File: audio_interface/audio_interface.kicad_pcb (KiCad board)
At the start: 2 copper layers, 139.7 x 81.3 mm, 152 parts, among them J1 XLR3, J10 MIC_EXT, J11 INST_EXT, J13 Test Headers, J14 SWD, J15 PCM_Jumper, J16 USB_B, J2 AudioJack2, J3 EXT_9V, J4 PROBE_GND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

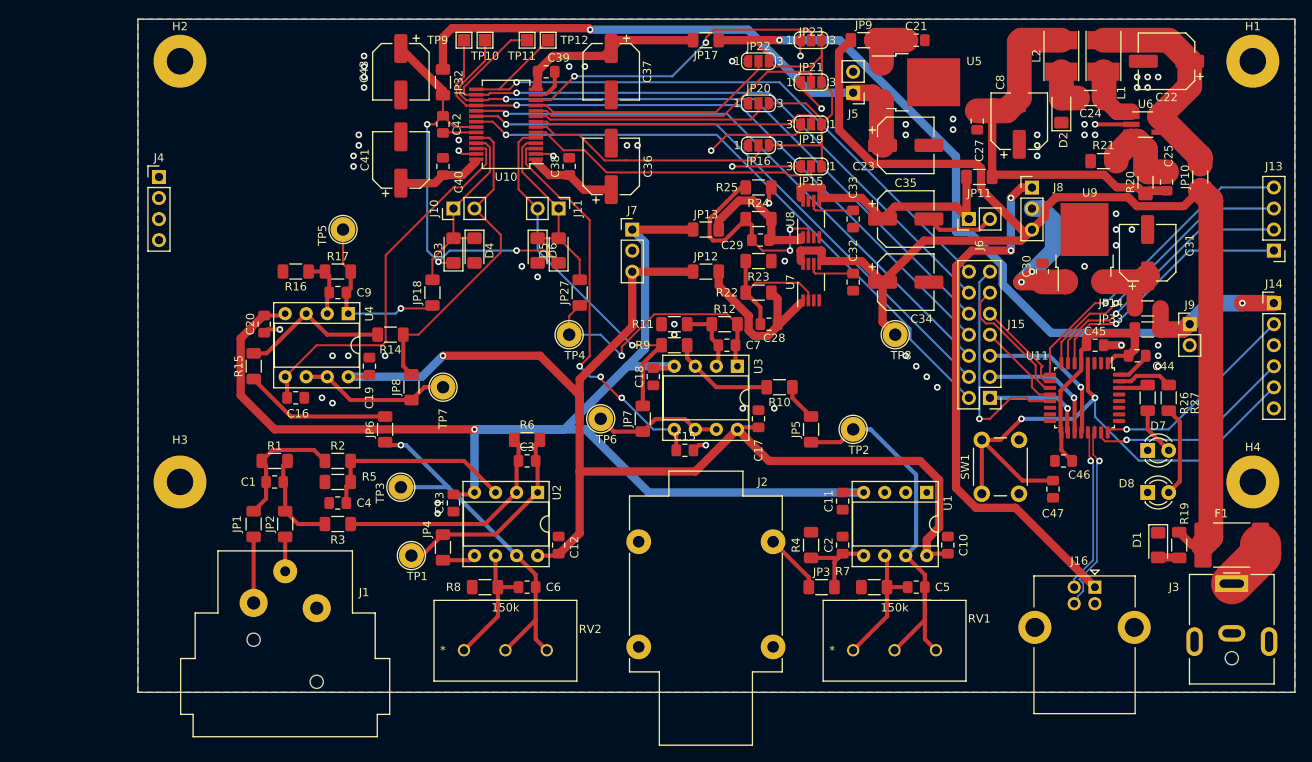
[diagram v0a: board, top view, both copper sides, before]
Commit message: Changed some footprints and grounding.
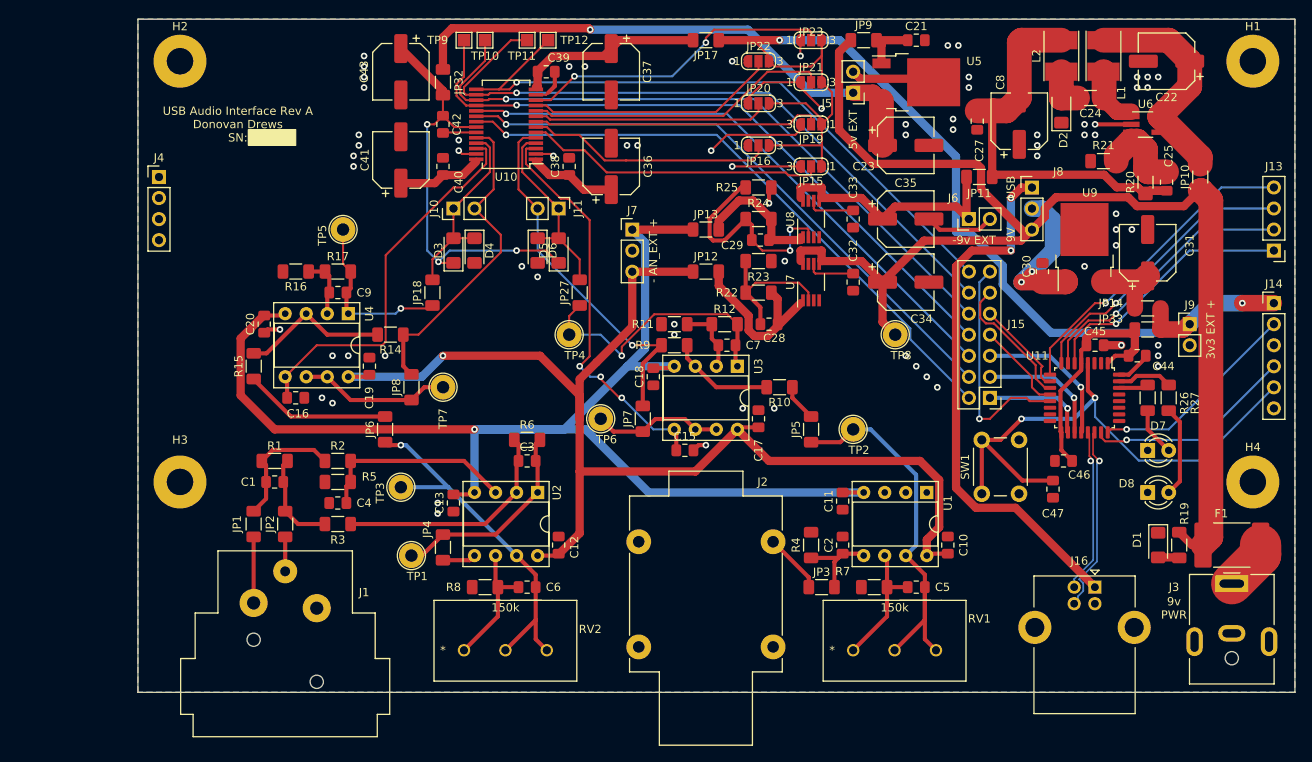
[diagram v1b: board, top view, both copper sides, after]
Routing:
- net GNDA: track 64.9 -> 82.9 mm, vias 66 -> 70
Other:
- board text added: "- AN_EXT +"
- board text added: "-9v EXT"
- board text added: "3v3 EXT +"
- board text added: "5v EXT"
- board text added: "9V"
- board text added: "9v PWR"
- board text added: "USB"
- board text added: "USB Audio Interface Rev A Donovan Drews SN:"
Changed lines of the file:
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@@
     (pad_to_mask_clearance 0)
     (pcbplotparams
-      (layerselection 0x0001030_ffffffff)
+      (layerselection 0x00010f0_ffffffff)
       (disableapertmacros false)
       (usegerberextensions false)
@@
       (sketchpadsonfab false)
       (subtractmaskfromsilk false)
-      (outputformat 4)
+      (outputformat 1)
       (mirror false)
       (drillshape 0)
       (scaleselection 1)
-      (outputdirectory "C:/Users/donsp/Documents/")
+      (outputdirectory "C:/Users/donsp/Documents/gerbs/")
     )
   )
@@
     (property "Sheetname" "Power")
     (attr through_hole)
-    (fp_text reference "J6" (at -3.175 1.27 90) (layer "F.SilkS")
+    (fp_text reference "J6" (at 2.54 -1.905 180) (layer "F.SilkS")
       (effects (font (size 1 1) (thickness 0.15)))
     )
@@
     (property "Sheetname" "Power")
     (attr through_hole)
-    (fp_text reference "J8" (at 3.175 -0.015) (layer "F.SilkS")
+    (fp_text reference "J8" (at 3.175 -1.92) (layer "F.SilkS")
       (effects (font (size 1 1) (thickness 0.15)))
     )
@@
     (property "Sheetname" "Power")
     (attr through_hole)
-    (fp_text reference "J5" (at 0 -2.54) (layer "F.SilkS")
+    (fp_text reference "J5" (at 3.175 -1.27) (layer "F.SilkS")
       (effects (font (size 1 1) (thickness 0.15)))
     )
@@
     )
   )
+  (gr_rect (start 140.335 94.615) (end 146.05 96.52) (layer "F.SilkS") (width 0.15) (fill solid))
   (gr_line (start 127 162.56) (end 127 81.28) (layer "Edge.Cuts") (width 0.1))
   (gr_line (start 266.7 81.28) (end 127 81.28) (layer "Edge.Cuts") (width 0.1))
   (gr_line (start 266.7 162.56) (end 266.7 81.28) (layer "Edge.Cuts") (width 0.1))
   (gr_line (start 127 162.56) (end 266.7 162.56) (layer "Edge.Cuts") (width 0.1))
+  (gr_text "5v EXT" (at 213.36 94.615 90) (layer "F.SilkS")
+    (effects (font (size 1 1) (thickness 0.15)))
+  )
+  (gr_text "3v3 EXT +" (at 256.54 118.745 90) (layer "F.SilkS")
+    (effects (font (size 1 1) (thickness 0.15)))
+  )
+  (gr_text "USB Audio Interface Rev A\nDonovan Drews\nSN:" (at 139.065 93.98) (layer "F.SilkS")
+    (effects (font (size 1 1) (thickness 0.15)))
+  )
+  (gr_text "- AN_EXT +" (at 189.23 109.22 90) (layer "F.SilkS")
+    (effects (font (size 1 1) (thickness 0.15)))
+  )
+  (gr_text "-9v EXT" (at 227.965 107.95) (layer "F.SilkS")
+    (effects (font (size 1 1) (thickness 0.15)))
+  )
+  (gr_text "9v\nPWR" (at 252.095 152.4) (layer "F.SilkS")
+    (effects (font (size 1 1) (thickness 0.15)))
+  )
+  (gr_text "9V" (at 232.41 107.315 90) (layer "F.SilkS")
+    (effects (font (size 1 1) (thickness 0.15)))
+  )
+  (gr_text "USB" (at 232.41 101.6 90) (layer "F.SilkS")
+    (effects (font (size 1 1) (thickness 0.15)))
+  )
   (segment (start 148.25548 133.29548) (end 143.28452 133.29548) (width 0.5) (layer "F.Cu") (net 1))
   (segment (start 142.4725 137.16) (end 142.4725 139.1875) (width 0.5) (layer "F.Cu") (net 1))
@@
   (segment (start 211.1 146.8075) (end 212.09 145.8175) (width 0.5) (layer "F.Cu") (net 3))
   (segment (start 208.28 146.33) (end 211.5775 146.33) (width 0.5) (layer "F.Cu") (net 3))
+  (segment (start 222.65048 88.47048) (end 223.08 88.9) (width 1) (layer "F.Cu") (net 4))
   (segment (start 206.98 89.505) (end 206.98 88.9) (width 0.25) (layer "F.Cu") (net 4))
+  (segment (start 200.63 90.835) (end 202.565 88.9) (width 0.25) (layer "F.Cu") (net 4))
   (segment (start 176.295 90.405) (end 176.53 90.17) (width 0.25) (layer "F.Cu") (net 4))
   (segment (start 203.2 103.505) (end 203.2 101.88) (width 0.5) (layer "F.Cu") (net 4))
   (segment (start 248.6875 121.92) (end 248.6875 122.1525) (width 0.5) (layer "F.Cu") (net 4))
+  (segment (start 202.565 88.9) (end 206.98 88.9) (width 0.25) (layer "F.Cu") (net 4))
   (segment (start 209.55 92.075) (end 206.98 89.505) (width 0.25) (layer "F.Cu") (net 4))
   (segment (start 206.98 94.645) (end 206.98 93.98) (width 0.25) (layer "F.Cu") (net 4))
@@
   (segment (start 222.51 105.41) (end 223.809511 106.709511) (width 0.5) (layer "F.Cu") (net 4))
   (segment (start 163.8925 94.955) (end 167.85 94.955) (width 0.25) (layer "F.Cu") (net 4))
+  (segment (start 200.63 91.44) (end 200.63 90.835) (width 0.25) (layer "F.Cu") (net 4))
   (segment (start 177.335 89.365) (end 176.53 90.17) (width 0.5) (layer "F.Cu") (net 4))
   (segment (start 198.12 95.25) (end 206.375 95.25) (width 0.25) (layer "F.Cu") (net 4))
@@
   (segment (start 206.98 99.06) (end 198.755 99.06) (width 0.25) (layer "F.Cu") (net 4))
   (segment (start 246.64 124.2) (end 245.475 124.2) (width 0.5) (layer "F.Cu") (net 4))
+  (segment (start 213.36 87.63) (end 214.20048 88.47048) (width 1) (layer "F.Cu") (net 4))
   (segment (start 175.05 97.555) (end 176.93 97.555) (width 0.25) (layer "F.Cu") (net 4))
+  (segment (start 214.20048 88.47048) (end 222.65048 88.47048) (width 1) (layer "F.Cu") (net 4))
   (segment (start 206.98 83.82) (end 206.98 85.695) (width 0.25) (layer "F.Cu") (net 4))
   (segment (start 242.57 93.98) (end 246.95 93.98) (width 0.5) (layer "F.Cu") (net 4))
@@
   (via (at 196.215 97.155) (size 0.8) (drill 0.4) (layers "F.Cu" "B.Cu") (free) (net 4))
   (via (at 163.195 139.7) (size 0.8) (drill 0.4) (layers "F.Cu" "B.Cu") (free) (net 4))
+  (via (at 226.06 84.455) (size 0.8) (drill 0.4) (layers "F.Cu" "B.Cu") (free) (net 4))
   (via (at 242.57 93.98) (size 0.8) (drill 0.4) (layers "F.Cu" "B.Cu") (free) (net 4))
   (via (at 153.035 97.79) (size 0.8) (drill 0.4) (layers "F.Cu" "B.Cu") (free) (net 4))
@@
   (via (at 222.25 124.46) (size 0.8) (drill 0.4) (layers "F.Cu" "B.Cu") (free) (net 4))
   (via (at 219.71 95.25) (size 0.8) (drill 0.4) (layers "F.Cu" "B.Cu") (free) (net 4))
+  (via (at 227.33 89.535) (size 0.8) (drill 0.4) (layers "F.Cu" "B.Cu") (free) (net 4))
   (via (at 153.67 95.25) (size 0.8) (drill 0.4) (layers "F.Cu" "B.Cu") (free) (net 4))
   (via (at 220.98 123.19) (size 0.8) (drill 0.4) (layers "F.Cu" "B.Cu") (free) (net 4))
@@
   (via (at 186.055 96.52) (size 0.8) (drill 0.4) (layers "F.Cu" "B.Cu") (free) (net 4))
   (via (at 180.975 86.995) (size 0.8) (drill 0.4) (layers "F.Cu" "B.Cu") (free) (net 4))
+  (via (at 227.33 88.265) (size 0.8) (drill 0.4) (layers "F.Cu" "B.Cu") (free) (net 4))
   (via (at 248.92 89.535) (size 0.8) (drill 0.4) (layers "F.Cu" "B.Cu") (free) (net 4))
   (via (at 154.305 89.535) (size 0.8) (drill 0.4) (layers "F.Cu" "B.Cu") (free) (net 4))
@@
   (via (at 245.11 104.775) (size 0.8) (drill 0.4) (layers "F.Cu" "B.Cu") (free) (net 4))
   (via (at 209.55 92.075) (size 0.8) (drill 0.4) (layers "F.Cu" "B.Cu") (free) (net 4))
+  (via (at 224.79 84.455) (size 0.8) (drill 0.4) (layers "F.Cu" "B.Cu") (free) (net 4))
   (via (at 177.165 97.79) (size 0.8) (drill 0.4) (layers "F.Cu" "B.Cu") (free) (net 4))
   (via (at 245.11 108.585) (size 0.8) (drill 0.4) (layers "F.Cu" "B.Cu") (free) (net 4))
@@
   (segment (start 148.59 120.65) (end 144.78 124.46) (width 0.25) (layer "F.Cu") (net 19))
   (segment (start 156.91452 109.78548) (end 156.91452 120.232973) (width 0.25) (layer "F.Cu") (net 19))
-  (segment (start 216.78 86.62) (end 216.78 84.42) (width 3) (layer "F.Cu") (net 20))
-  (segment (start 216.18 83.82) (end 219.73048 83.82) (width 3) (layer "F.Cu") (net 20))
-  (segment (start 216.78 84.42) (end 216.18 83.82) (width 3) (layer "F.Cu") (net 20))
+  (segment (start 216.78 86.62) (end 216.78 84.42) (width 1) (layer "F.Cu") (net 20))
+  (segment (start 216.78 84.42) (end 216.18 83.82) (width 1) (layer "F.Cu") (net 20))
+  (segment (start 216.18 83.82) (end 219.9425 83.82) (width 1) (layer "F.Cu") (net 20))
   (segment (start 241.874999 131.349999) (end 241.7 131.175) (width 0.2) (layer "F.Cu") (net 21))
   (segment (start 241.874999 134.036396) (end 241.874999 131.349999) (width 0.2) (layer "F.Cu") (net 21))

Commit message: Changed pin mappings for easier layout. Redid layout for better ground plane.
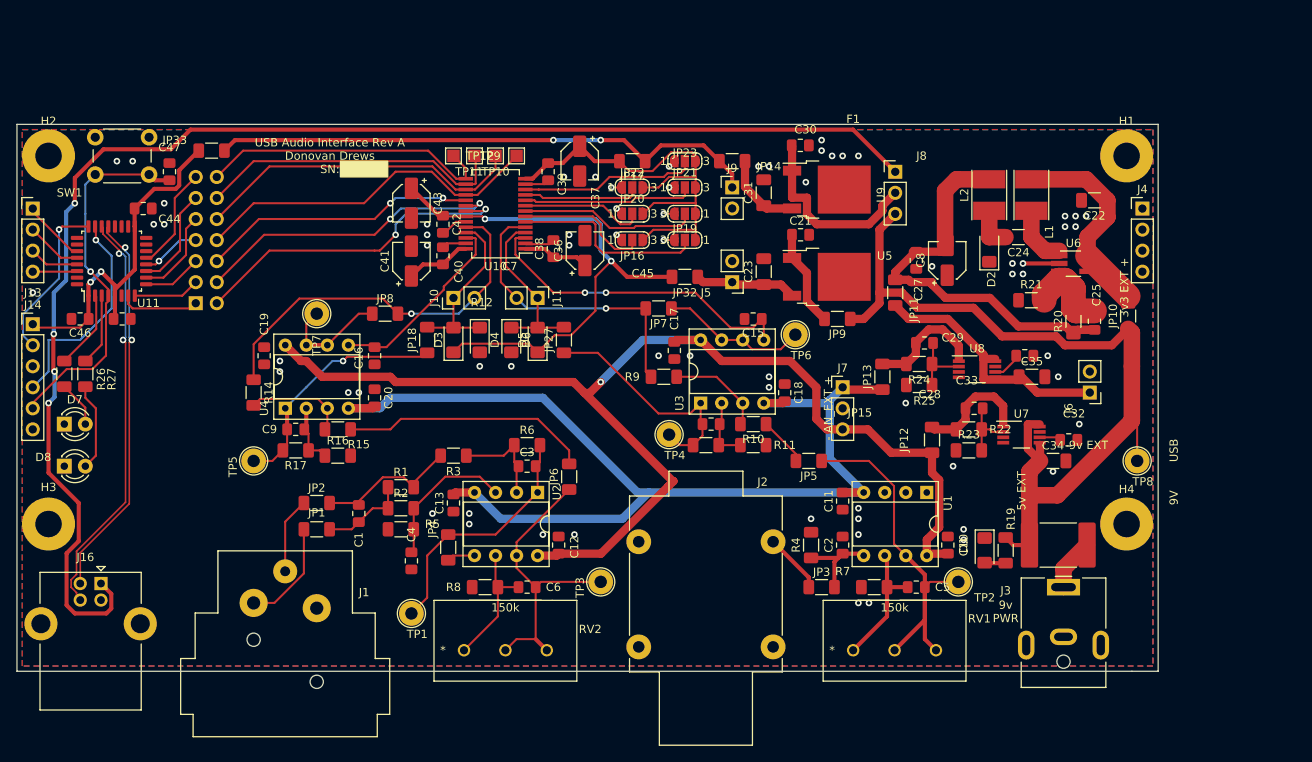
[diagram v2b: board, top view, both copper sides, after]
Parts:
- C22, C23, C31, C34, C35: footprint Capacitor_SMD:CP_Elec_6.3x5.2 -> Capacitor_SMD:C_1206_3216Metric_Pad1.33x1.80mm_HandSolder
- C36, C37, C41, C43, C8: footprint Capacitor_SMD:CP_Elec_6.3x5.2 -> Capacitor_SMD:CP_Elec_4x5.4
- J15: moved to B.Cu
- moved J13 149.9 mm to (114.3, 104.2), turned to 0 degrees
- moved J14 149.9 mm to (114.3, 118.1)
- moved D7 130.8 mm to (118.1, 130.2)
- moved D8 130.8 mm to (118.1, 135.3)
- moved R26 130.8 mm to (118.1, 124.1)
- moved R27 130.8 mm to (120.7, 124.1)
- moved C44 121.3 mm to (127.6, 104.1)
- moved J16 120.0 mm to (122.5, 149.4)
- moved C46 120.0 mm to (120.0, 117.5)
- moved J4 118.8 mm to (248.3, 104.2)
- moved U11 118.6 mm to (123.8, 110.5), turned to 90 degrees
- moved C45 117.5 mm to (125.1, 117.5)
- moved JP33 115.1 mm to (135.9, 97.2)
- moved C47 113.4 mm to (130.8, 99.7), turned to 90 degrees
- moved SW1 107.7 mm to (128.3, 100.0), turned to 180 degrees
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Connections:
- C37 pad 1: Net-(C37-Pad1) -> /Digital/ADC_3V3
- C39 pad 1: Net-(C37-Pad1) -> /Digital/ADC_3V3
- C44 pad 1: Net-(C44-Pad1) -> Net-(J14-Pad1)
- C45 pad 1: Net-(C44-Pad1) -> Net-(J14-Pad1)
- C46 pad 1: Net-(C44-Pad1) -> Net-(J14-Pad1)
- J14 pad 1: +3V3 -> Net-(J14-Pad1)
- JP15 pad 1: +3V3 -> /Digital/ADC_3V3
- JP16 pad 3: +3V3 -> /Digital/ADC_3V3
- JP17 pad 2: Net-(C37-Pad1) -> /Digital/ADC_3V3
- JP19 pad 1: +3V3 -> /Digital/ADC_3V3
- JP20 pad 3: +3V3 -> /Digital/ADC_3V3
- JP21 pad 3: +3V3 -> /Digital/ADC_3V3
- JP22 pad 3: +3V3 -> /Digital/ADC_3V3
- JP23 pad 3: +3V3 -> /Digital/ADC_3V3
- JP33 pad 1: Net-(C44-Pad1) -> Net-(J14-Pad1)
- R26 pad 1: Net-(R26-Pad1) -> Net-(U11-Pad2)
- R27 pad 1: Net-(R27-Pad1) -> Net-(U11-Pad3)
- U10 pad 14: Net-(C37-Pad1) -> /Digital/ADC_3V3
- U11 pad 1: Net-(C44-Pad1) -> Net-(J14-Pad1)
- U11 pad 17: Net-(C44-Pad1) -> Net-(J14-Pad1)
- U11 pad 18: /Digital/STM_CLIP_L -> unconnected-(U11-Pad18)
- U11 pad 19: /Digital/STM_CLIP_R -> unconnected-(U11-Pad19)
- U11 pad 2: unconnected-(U11-Pad2) -> Net-(U11-Pad2)
- U11 pad 20: /Digital/STM_PCM_RST_n -> unconnected-(U11-Pad20)
- U11 pad 27: unconnected-(U11-Pad27) -> Net-(J13-Pad1)
- U11 pad 28: unconnected-(U11-Pad28) -> Net-(J13-Pad2)
- U11 pad 29: unconnected-(U11-Pad29) -> Net-(J13-Pad3)
- U11 pad 3: unconnected-(U11-Pad3) -> Net-(U11-Pad3)
- U11 pad 30: Net-(R26-Pad1) -> Net-(J13-Pad4)
- U11 pad 31: Net-(R27-Pad1) -> unconnected-(U11-Pad31)
- U11 pad 5: Net-(C44-Pad1) -> Net-(J14-Pad1)
- U11 pad 6: Net-(J13-Pad1) -> unconnected-(U11-Pad6)
- U11 pad 7: Net-(J13-Pad2) -> /Digital/STM_CLIP_L
- U11 pad 8: Net-(J13-Pad3) -> /Digital/STM_CLIP_R
- U11 pad 9: Net-(J13-Pad4) -> /Digital/STM_PCM_RST_n
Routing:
- net USB_5V: track 65.3 -> 168.3 mm, vias 2 -> 4
- net +3V3: track 142.9 -> 66.7 mm
- net GNDA: track 82.9 -> 24.2 mm, vias 70 -> 67
- net /Digital/ADC_3V3: track 0.00 -> 55.9 mm
- net +5VA: track 66.3 -> 12.3 mm, vias 1 -> 0
- net +9V: track 153.6 -> 104.2 mm
- net /Digital/I2S_CLK: track 81.8 -> 37.7 mm, vias 1 -> 0
- net Net-(J14-Pad1): track 0.00 -> 43.4 mm, vias 0 -> 2
- net /Digital/I2S_SD: track 77.7 -> 36.2 mm, vias 1 -> 0
- net /Digital/I2S_WS: track 80.3 -> 40.1 mm, vias 1 -> 0
- net /Digital/PCM_RST_n: track 71.7 -> 33.3 mm, vias 1 -> 2
- net /Digital/PCM_CLK: track 80.9 -> 42.7 mm, vias 1 -> 0
- net /Digital/CLIP_R: track 72.5 -> 37.5 mm, vias 1 -> 2
- net /Digital/CLIP_L: track 74.1 -> 40.4 mm, vias 1 -> 2
- net Net-(J13-Pad4): track 38.3 -> 5.38 mm, vias 1 -> 0
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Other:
- board size 139.7 x 81.3 mm -> 137.8 x 66 mm

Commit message: Fixed some footprints, fixed silkscreen.
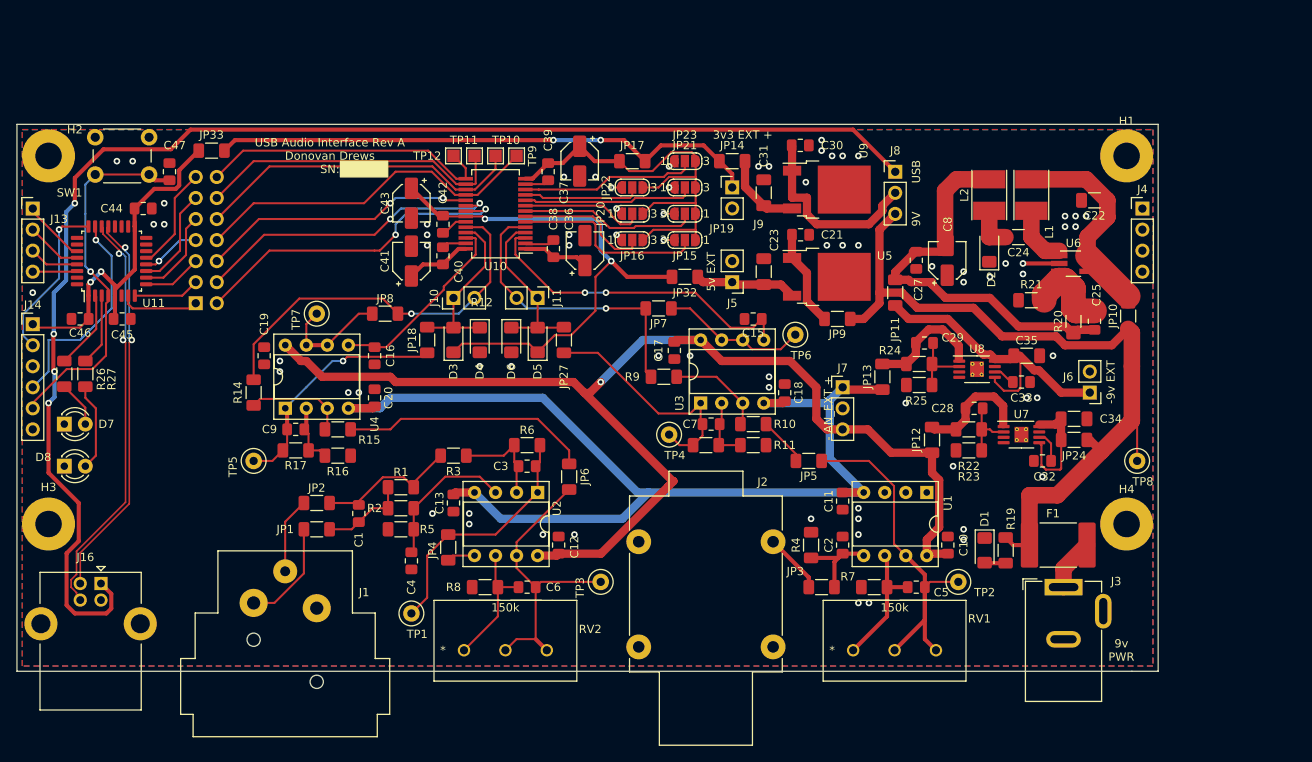
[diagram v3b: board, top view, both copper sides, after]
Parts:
- added JP24: Jumper_2_Bridged, Resistor_SMD:R_1206_3216Metric_Pad1.30x1.75mm_HandSolder, F.Cu at (240.0, 132.1)
- J3: footprint Connector_BarrelJack:BarrelJack_CUI_PJ-063AH_Horizontal -> Connector_BarrelJack:BarrelJack_GCT_DCJ200-10-A_Horizontal
- TP1, TP2, TP3, TP4, TP5, TP6, TP7, TP8: footprint TestPoint:TestPoint_Loop_D2.54mm_Drill1.5mm_Beaded -> TestPoint:TestPoint_Loop_D2.50mm_Drill1.0mm
- U7, U8: footprint Package_SO:VSSOP-8_3.0x3.0mm_P0.65mm -> Package_SO:MSOP-8-1EP_3x3mm_P0.65mm_EP1.68x1.88mm_ThermalVias
- moved C34 5.68 mm to (240.0, 129.5)
- moved C32 4.07 mm to (236.2, 134.6), turned to 180 degrees
- moved C33 3.20 mm to (233.7, 125.1)
- moved C35 2.62 mm to (234.3, 121.9)
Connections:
- C34 pad 1: +9V -> Net-(C34-Pad1)
- U7 pad 5: +9V -> Net-(C34-Pad1)
- U7 pad 8: +9V -> Net-(C34-Pad1)
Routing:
- net Net-(C34-Pad1): track 0.00 -> 14.4 mm
- net +9V: track 104.2 -> 93.4 mm
- net -9V: track 31.3 -> 36.6 mm
- net Net-(C32-Pad1): track 2.61 -> 3.84 mm
- net Net-(C33-Pad1): track 3.56 -> 2.68 mm
- net GNDA: vias 67 -> 72
